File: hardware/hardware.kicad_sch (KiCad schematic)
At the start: 37 parts, among them J1 Conn_01x06, J2 Conn_01x02, J3 Conn_01x03, J4 USB_C_Receptacle_USB2.0_14P, J5 Conn_01x03, J6 RJ45, J7 RJ45, Q1 BSS138, Q2 BSS138, U1 CH340C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

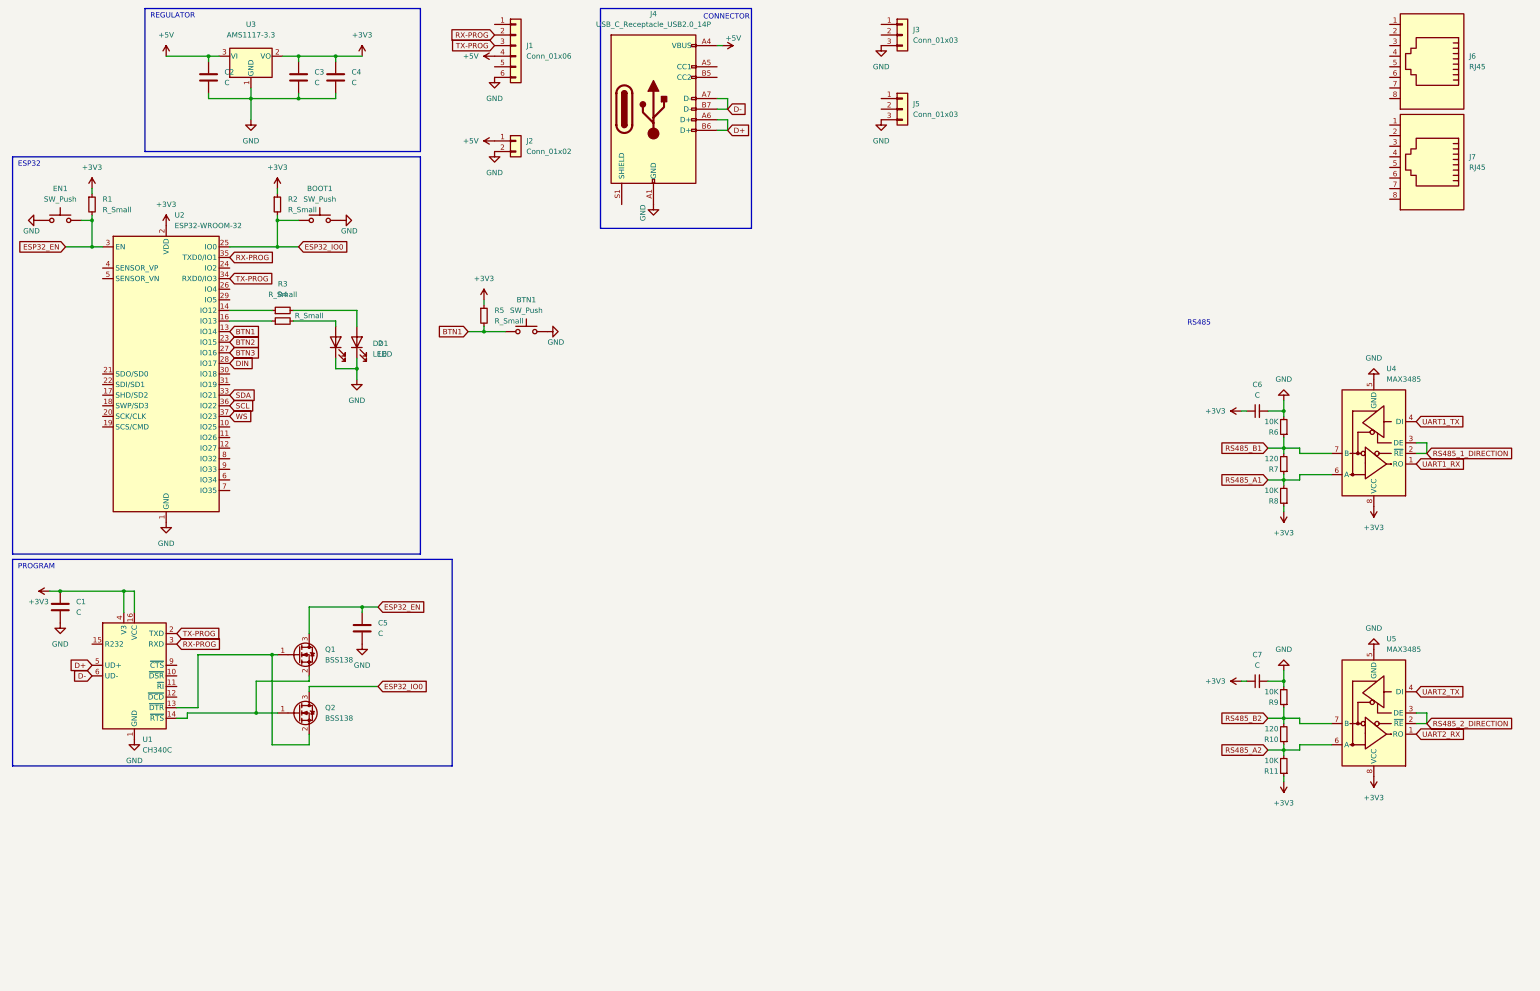
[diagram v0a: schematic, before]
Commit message: add pcb wiring
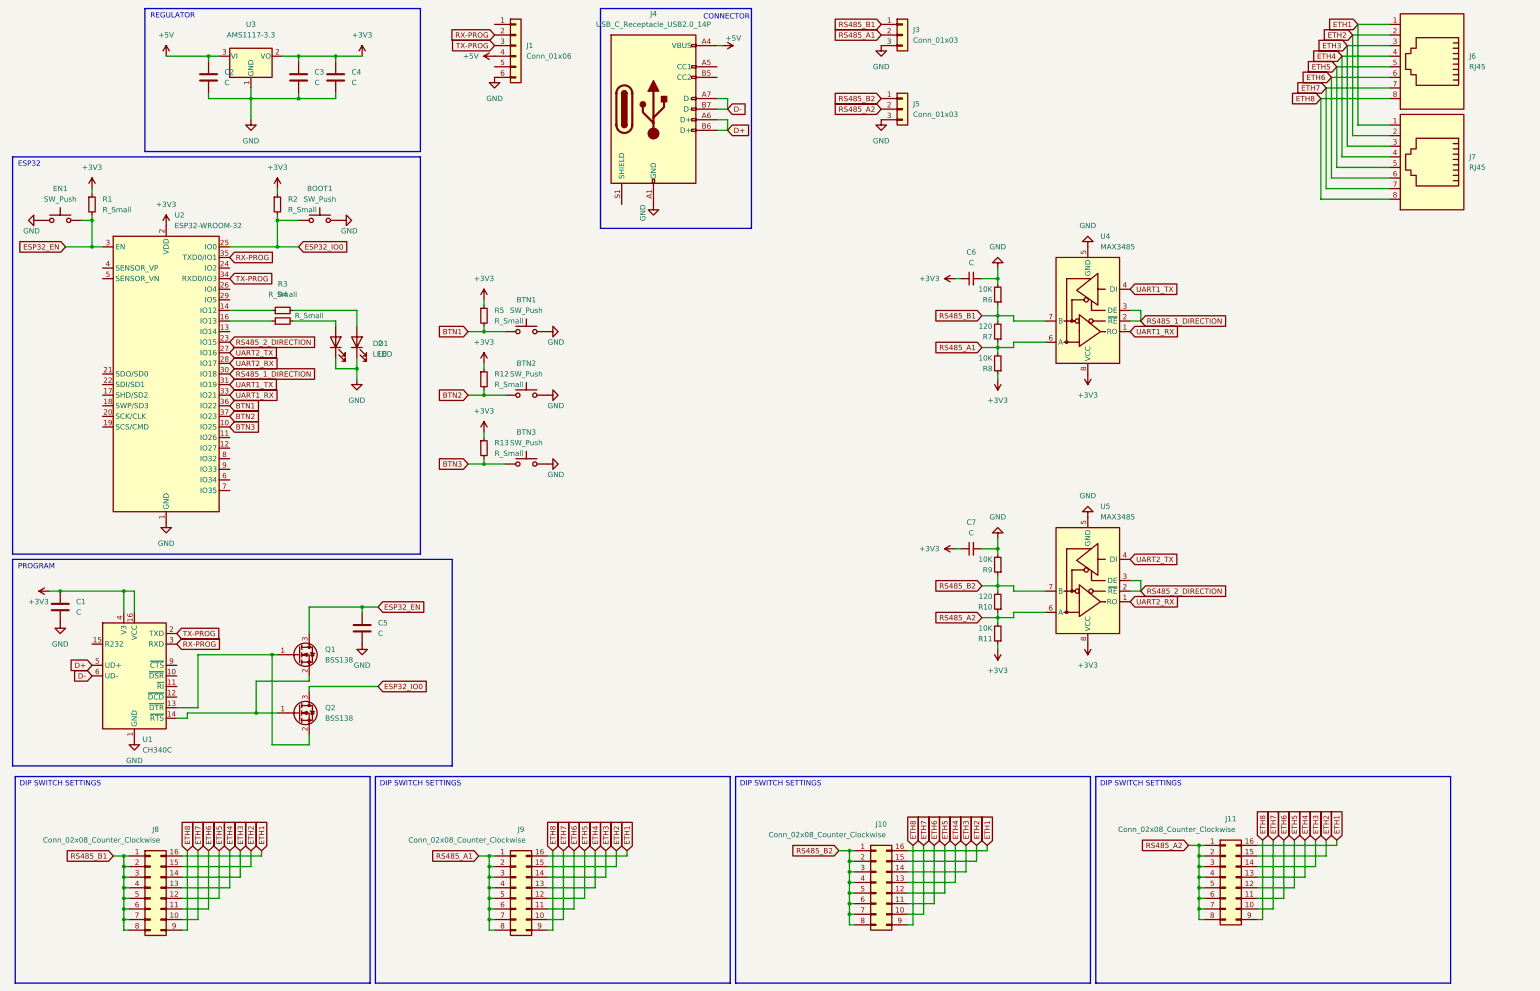
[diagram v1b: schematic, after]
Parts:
- removed J2: Conn_01x02, Connector_PinSocket_2.54mm:PinSocket_1x02_P2.54mm_Vertical, symbol Connector_Generic:Conn_01x02
- added BTN2, BTN3: SW_Push, Button_Switch_SMD:SW_SPST_FSMSM, symbol Switch:SW_Push
- added J10, J11, J8, J9: Conn_02x08_Counter_Clockwise, Button_Switch_SMD:SW_DIP_SPSTx08_Slide_6.7x21.88mm_W8.61mm_P2.54mm_LowProfile, symbol Connector_Generic:Conn_02x08_Counter_Clockwise
- added R12, R13: R_Small, Resistor_SMD:R_0603_1608Metric, symbol Device:R_Small
- J6, J7: footprint (none) -> Connector_RJ:RJ45_Amphenol_RJHSE5380
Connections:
- net DIN is gone; now on net UART2_RX: U2.28 (IO17)
- net SCL is gone; now on net BTN1: U2.36 (IO22)
- net SDA is gone; now on net UART1_RX: U2.33 (IO21)
- net WS is gone; now on net BTN2: U2.37 (IO23)
- net +3V3: now also R12.1, R13.1
- net BTN1: no longer U2.13 (IO14)
- net BTN2: now also BTN2.1, R12.2; no longer U2.23 (IO15)
- net BTN3: now also U2.10 (IO25), BTN3.1, R13.2; no longer U2.27 (IO16)
- net GND: now also BTN2.2, BTN3.2
- net RS485_1_DIRECTION: now also U2.30 (IO18)
- net RS485_2_DIRECTION: now also U2.23 (IO15)
- net RS485_A1: now also J3.2 (Pin_2), J9.1 (Pin_1), J9.2 (Pin_2), J9.3 (Pin_3), J9.4 (Pin_4), J9.5 (Pin_5), J9.6 (Pin_6), J9.7 (Pin_7), J9.8 (Pin_8)
- net RS485_A2: now also J5.2 (Pin_2), J11.1 (Pin_1), J11.2 (Pin_2), J11.3 (Pin_3), J11.4 (Pin_4), J11.5 (Pin_5), J11.6 (Pin_6), J11.7 (Pin_7), J11.8 (Pin_8)
- net RS485_B1: now also J3.1 (Pin_1), J8.1 (Pin_1), J8.2 (Pin_2), J8.3 (Pin_3), J8.4 (Pin_4), J8.5 (Pin_5), J8.6 (Pin_6), J8.7 (Pin_7), J8.8 (Pin_8)
- net RS485_B2: now also J5.1 (Pin_1), J10.1 (Pin_1), J10.2 (Pin_2), J10.3 (Pin_3), J10.4 (Pin_4), J10.5 (Pin_5), J10.6 (Pin_6), J10.7 (Pin_7), J10.8 (Pin_8)
- net UART1_TX: now also U2.31 (IO19)
- net UART2_TX: now also U2.27 (IO16)
- net ETH1: now reaches J7.1
- net ETH1: now also J6.1, J10.16 (Pin_16), J11.16 (Pin_16), J8.16 (Pin_16), J9.16 (Pin_16)
- net ETH2: now reaches J7.2
- net ETH2: now also J6.2, J10.15 (Pin_15), J11.15 (Pin_15), J8.15 (Pin_15), J9.15 (Pin_15)
- net ETH3: now reaches J7.3
- net ETH3: now also J6.3, J10.14 (Pin_14), J11.14 (Pin_14), J8.14 (Pin_14), J9.14 (Pin_14)
- net ETH4: now reaches J7.4
- net ETH4: now also J6.4, J10.13 (Pin_13), J11.13 (Pin_13), J8.13 (Pin_13), J9.13 (Pin_13)
- net ETH5: now reaches J7.5
- net ETH5: now also J6.5, J10.12 (Pin_12), J11.12 (Pin_12), J8.12 (Pin_12), J9.12 (Pin_12)
- net ETH6: now reaches J7.6
- net ETH6: now also J6.6, J10.11 (Pin_11), J11.11 (Pin_11), J8.11 (Pin_11), J9.11 (Pin_11)
- net ETH7: now reaches J7.7
- net ETH7: now also J6.7, J10.10 (Pin_10), J11.10 (Pin_10), J8.10 (Pin_10), J9.10 (Pin_10)
- net ETH8: now reaches J7.8
- net ETH8: now also J6.8, J10.9 (Pin_9), J11.9 (Pin_9), J8.9 (Pin_9), J9.9 (Pin_9)
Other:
- note added: "DIP SWITCH SETTINGS"
- note removed: "RS485"
- moved on the sheet: C6, C7, R10, R11, R6, R7, R8, R9, U4, U5
